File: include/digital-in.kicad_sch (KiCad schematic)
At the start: 6 parts, among them U9 EL817

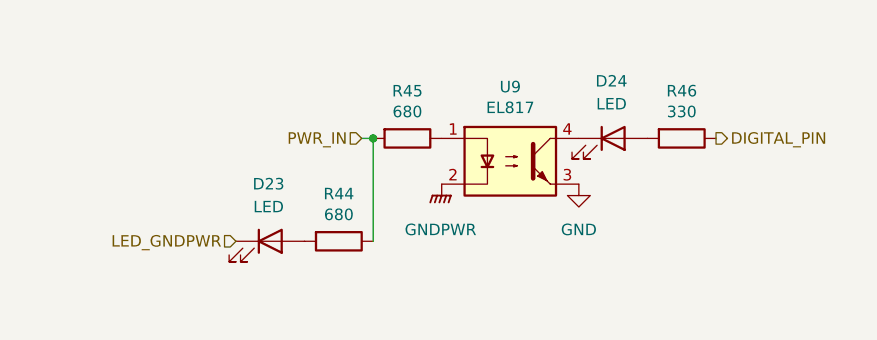
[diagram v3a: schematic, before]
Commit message: refactoring slave-8in-8out
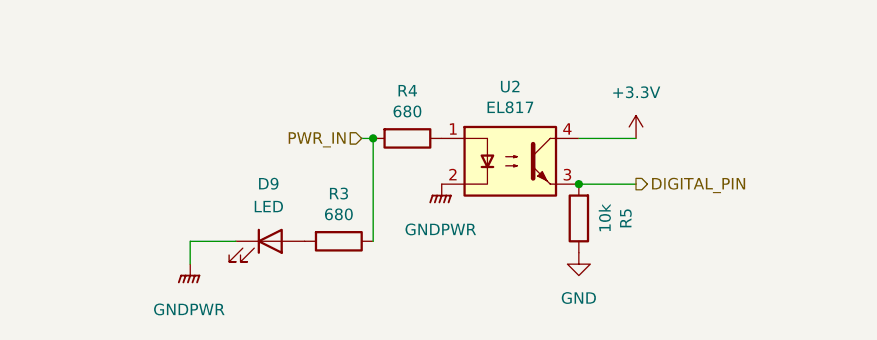
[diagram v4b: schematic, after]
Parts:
- removed D24: LED, Resistor_SMD:R_0805_2012Metric, symbol Device:LED
- R5: renamed from R46; value 330 -> 10k; LCSC C25117 -> C25744
- renumbered D23 to D9, R44 to R3, R45 to R4, U9 to U2
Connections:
- net LED_GNDPWR is gone; now on net GNDPWR: D9.1 (K)
- net DIGITAL_PIN: now also R5.2, U2.3; no longer R5.1
- net GND: now also R5.1; no longer U2.3
- net +3V3: now reaches U2.4
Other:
- moved on the sheet: R5
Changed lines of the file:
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@@
   (paper "A4")
   (junction (at 74.93 36.83) (diameter 0.9144) (color 0 0 0 0))
+  (junction (at 97.79 41.91) (diameter 0) (color 0 0 0 0))
+  (wire (pts (xy 54.61 48.26) (xy 54.61 50.8))
+    (stroke (width 0) (type default) (color 0 0 0 0))
+  )
+  (wire (pts (xy 59.69 48.26) (xy 54.61 48.26))
+    (stroke (width 0) (type default) (color 0 0 0 0))
+  )
   (wire (pts (xy 73.66 36.83) (xy 74.93 36.83))
     (stroke (width 0) (type solid) (color 0 0 0 0))
@@
     (stroke (width 0) (type solid) (color 0 0 0 0))
   )
-  (hierarchical_label "LED_GNDPWR" (shape input) (at 59.69 48.26 180)
-    (effects (font (size 1.27 1.27)) (justify right))
+  (wire (pts (xy 97.79 36.83) (xy 104.14 36.83))
+    (stroke (width 0) (type default) (color 0 0 0 0))
+  )
+  (wire (pts (xy 97.79 41.91) (xy 104.14 41.91))
+    (stroke (width 0) (type default) (color 0 0 0 0))
   )
   (hierarchical_label "PWR_IN" (shape input) (at 73.66 36.83 180)
     (effects (font (size 1.27 1.27)) (justify right))
   )
-  (hierarchical_label "DIGITAL_PIN" (shape output) (at 113.03 36.83 0)
+  (hierarchical_label "DIGITAL_PIN" (shape output) (at 104.14 41.91 0)
     (effects (font (size 1.27 1.27)) (justify left))
+  )
+  (symbol (lib_id "power:+3.3V") (at 104.14 36.83 0)
+    (in_bom yes) (on_board yes) (fields_autoplaced)
+    (property "Reference" "#PWR0126" (id 0) (at 104.14 40.64 0)
+      (effects (font (size 1.27 1.27)) hide)
+    )
+    (property "Value" "+3.3V" (id 1) (at 104.14 31.75 0))
+    (property "Footprint" "" (id 2) (at 104.14 36.83 0)
+      (effects (font (size 1.27 1.27)) hide)
+    )
+    (property "Datasheet" "" (id 3) (at 104.14 36.83 0)
+      (effects (font (size 1.27 1.27)) hide)
+    )
+    (pin "1")
+  )
+  (symbol (lib_id "power:GNDPWR") (at 54.61 50.8 0)
+    (in_bom yes) (on_board yes) (fields_autoplaced)
+    (property "Reference" "#PWR0134" (id 0) (at 54.61 55.88 0)
+      (effects (font (size 1.27 1.27)) hide)
+    )
+    (property "Value" "GNDPWR" (id 1) (at 54.483 55.88 0))
+    (property "Footprint" "" (id 2) (at 54.61 52.07 0)
+      (effects (font (size 1.27 1.27)) hide)
+    )
+    (property "Datasheet" "" (id 3) (at 54.61 52.07 0)
+      (effects (font (size 1.27 1.27)) hide)
+    )
+    (pin "1")
   )
   (symbol (lib_id "power:GNDPWR") (at 82.55 41.91 0)
@@
     (pin "1")
   )
-  (symbol (lib_id "power:GND") (at 97.79 41.91 0)
+  (symbol (lib_id "power:GND") (at 97.79 49.53 0)
     (in_bom yes) (on_board yes) (fields_autoplaced)
-    (property "Reference" "#PWR0116" (id 0) (at 97.79 48.26 0)
+    (property "Reference" "#PWR0116" (id 0) (at 97.79 55.88 0)
       (effects (font (size 1.27 1.27)) hide)
     )
-    (property "Value" "GND" (id 1) (at 97.79 46.99 0))
-    (property "Footprint" "" (id 2) (at 97.79 41.91 0)
+    (property "Value" "GND" (id 1) (at 97.79 54.61 0))
+    (property "Footprint" "" (id 2) (at 97.79 49.53 0)
       (effects (font (size 1.27 1.27)) hide)
     )
-    (property "Datasheet" "" (id 3) (at 97.79 41.91 0)
+    (property "Datasheet" "" (id 3) (at 97.79 49.53 0)
       (effects (font (size 1.27 1.27)) hide)
     )
@@
   (symbol (lib_id "Device:R") (at 71.12 48.26 270)
     (in_bom yes) (on_board yes)
-    (property "Reference" "R44" (id 0) (at 71.12 43.0022 90))
+    (property "Reference" "R3" (id 0) (at 71.12 43.0022 90))
     (property "Value" "680" (id 1) (at 71.12 45.3136 90))
     (property "Footprint" "Resistor_SMD:R_0402_1005Metric" (id 2) (at 71.12 46.482 90)
@@
   (symbol (lib_id "Device:R") (at 78.74 36.83 270)
     (in_bom yes) (on_board yes)
-    (property "Reference" "R45" (id 0) (at 78.74 31.5722 90))
+    (property "Reference" "R4" (id 0) (at 78.74 31.5722 90))
     (property "Value" "680" (id 1) (at 78.74 33.8836 90))
     (property "Footprint" "Resistor_SMD:R_0402_1005Metric" (id 2) (at 78.74 35.052 90)
@@
     (pin "2")
   )
-  (symbol (lib_id "Device:R") (at 109.22 36.83 270)
+  (symbol (lib_id "Device:R") (at 97.79 45.72 180)
     (in_bom yes) (on_board yes)
-    (property "Reference" "R46" (id 0) (at 109.22 31.5722 90))
-    (property "Value" "330" (id 1) (at 109.22 33.8836 90))
-    (property "Footprint" "Resistor_SMD:R_0402_1005Metric" (id 2) (at 109.22 35.052 90)
+    (property "Reference" "R5" (id 0) (at 103.0478 45.72 90))
+    (property "Value" "10k" (id 1) (at 100.7364 45.72 90))
+    (property "Footprint" "Resistor_SMD:R_0402_1005Metric" (id 2) (at 99.568 45.72 90)
       (effects (font (size 1.27 1.27)) hide)
     )
-    (property "Datasheet" "https://datasheet.lcsc.com/lcsc/1810170414_UNI-ROYAL-Uniroyal-Elec-0402WGF4700TCE_C25117.pdf" (id 3) (at 109.22 36.83 0)
+    (property "Datasheet" "https://datasheet.lcsc.com/lcsc/1809301717_UNI-ROYAL-Uniroyal-Elec-0402WGF1002TCE_C25744.pdf" (id 3) (at 97.79 45.72 0)
       (effects (font (size 1.27 1.27)) hide)
     )
-    (property "LCSC" "C25117" (id 4) (at 109.22 36.83 90)
+    (property "LCSC" "C25744" (id 4) (at 97.79 45.72 90)
       (effects (font (size 1.27 1.27)) hide)
     )
@@
   (symbol (lib_id "Device:LED") (at 63.5 48.26 0)
     (in_bom yes) (on_board yes) (fields_autoplaced)
-    (property "Reference" "D23" (id 0) (at 63.3095 41.91 0))
+    (property "Reference" "D9" (id 0) (at 63.3095 41.91 0))
     (property "Value" "LED" (id 1) (at 63.3095 44.45 0))
     (property "Footprint" "Resistor_SMD:R_0805_2012Metric" (id 2) (at 63.5 48.26 0)
@@
     (pin "2")
   )
-  (symbol (lib_id "Device:LED") (at 101.6 36.83 0)
-    (in_bom yes) (on_board yes) (fields_autoplaced)
-    (property "Reference" "D24" (id 0) (at 101.4095 30.48 0))
-    (property "Value" "LED" (id 1) (at 101.4095 33.02 0))
-    (property "Footprint" "Resistor_SMD:R_0805_2012Metric" (id 2) (at 101.6 36.83 0)
-      (effects (font (size 1.27 1.27)) hide)
-    )
-    (property "Datasheet" "https://datasheet.lcsc.com/lcsc/2008201032_Foshan-NationStar-Optoelectronics-NCD0805R1_C84256.pdf" (id 3) (at 101.6 36.83 0)
-      (effects (font (size 1.27 1.27)) hide)
-    )
-    (property "LCSC" "C84256" (id 4) (at 101.6 36.83 0)
-      (effects (font (size 1.27 1.27)) hide)
-    )
-    (pin "1")
-    (pin "2")
-  )
   (symbol (lib_id "jlcpcb:EL817") (at 90.17 39.37 0)
     (in_bom yes) (on_board yes)
-    (property "Reference" "U9" (id 0) (at 90.17 31.115 0))
+    (property "Reference" "U2" (id 0) (at 90.17 31.115 0))
     (property "Value" "EL817" (id 1) (at 90.17 33.4264 0))
     (property "Footprint" "jlcpcb:EL817" (id 2) (at 111.76 44.45 0)

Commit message: update slave-8in-8out
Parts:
- renumbered D9 to D23, R3 to R44, R4 to R45, R5 to R46, U2 to U9
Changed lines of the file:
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@@
   (symbol (lib_id "Device:R") (at 71.12 48.26 270)
     (in_bom yes) (on_board yes)
-    (property "Reference" "R3" (id 0) (at 71.12 43.0022 90))
+    (property "Reference" "R44" (id 0) (at 71.12 43.0022 90))
     (property "Value" "680" (id 1) (at 71.12 45.3136 90))
     (property "Footprint" "Resistor_SMD:R_0402_1005Metric" (id 2) (at 71.12 46.482 90)
@@
   (symbol (lib_id "Device:R") (at 78.74 36.83 270)
     (in_bom yes) (on_board yes)
-    (property "Reference" "R4" (id 0) (at 78.74 31.5722 90))
+    (property "Reference" "R45" (id 0) (at 78.74 31.5722 90))
     (property "Value" "680" (id 1) (at 78.74 33.8836 90))
     (property "Footprint" "Resistor_SMD:R_0402_1005Metric" (id 2) (at 78.74 35.052 90)
@@
   (symbol (lib_id "Device:R") (at 97.79 45.72 180)
     (in_bom yes) (on_board yes)
-    (property "Reference" "R5" (id 0) (at 103.0478 45.72 90))
+    (property "Reference" "R46" (id 0) (at 103.0478 45.72 90))
     (property "Value" "10k" (id 1) (at 100.7364 45.72 90))
     (property "Footprint" "Resistor_SMD:R_0402_1005Metric" (id 2) (at 99.568 45.72 90)
@@
   (symbol (lib_id "Device:LED") (at 63.5 48.26 0)
     (in_bom yes) (on_board yes) (fields_autoplaced)
-    (property "Reference" "D9" (id 0) (at 63.3095 41.91 0))
+    (property "Reference" "D23" (id 0) (at 63.3095 41.91 0))
     (property "Value" "LED" (id 1) (at 63.3095 44.45 0))
     (property "Footprint" "Resistor_SMD:R_0805_2012Metric" (id 2) (at 63.5 48.26 0)
@@
   (symbol (lib_id "jlcpcb:EL817") (at 90.17 39.37 0)
     (in_bom yes) (on_board yes)
-    (property "Reference" "U2" (id 0) (at 90.17 31.115 0))
+    (property "Reference" "U9" (id 0) (at 90.17 31.115 0))
     (property "Value" "EL817" (id 1) (at 90.17 33.4264 0))
     (property "Footprint" "jlcpcb:EL817" (id 2) (at 111.76 44.45 0)

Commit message: update slave-8in-8out
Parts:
- renumbered D23 to D9, R44 to R3, R45 to R4, R46 to R5, U9 to U2
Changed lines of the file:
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@@
   (symbol (lib_id "power:+3.3V") (at 104.14 36.83 0)
     (in_bom yes) (on_board yes) (fields_autoplaced)
-    (property "Reference" "#PWR0126" (id 0) (at 104.14 40.64 0)
+    (property "Reference" "#PWR0119" (id 0) (at 104.14 40.64 0)
       (effects (font (size 1.27 1.27)) hide)
     )
@@
   (symbol (lib_id "power:GNDPWR") (at 54.61 50.8 0)
     (in_bom yes) (on_board yes) (fields_autoplaced)
-    (property "Reference" "#PWR0134" (id 0) (at 54.61 55.88 0)
+    (property "Reference" "#PWR0127" (id 0) (at 54.61 55.88 0)
       (effects (font (size 1.27 1.27)) hide)
     )
@@
   (symbol (lib_id "power:GNDPWR") (at 82.55 41.91 0)
     (in_bom yes) (on_board yes) (fields_autoplaced)
-    (property "Reference" "#PWR0115" (id 0) (at 82.55 46.99 0)
+    (property "Reference" "#PWR0101" (id 0) (at 82.55 46.99 0)
       (effects (font (size 1.27 1.27)) hide)
     )
@@
   (symbol (lib_id "power:GND") (at 97.79 49.53 0)
     (in_bom yes) (on_board yes) (fields_autoplaced)
-    (property "Reference" "#PWR0116" (id 0) (at 97.79 55.88 0)
+    (property "Reference" "#PWR0102" (id 0) (at 97.79 55.88 0)
       (effects (font (size 1.27 1.27)) hide)
     )
@@
   (symbol (lib_id "Device:R") (at 71.12 48.26 270)
     (in_bom yes) (on_board yes)
-    (property "Reference" "R44" (id 0) (at 71.12 43.0022 90))
+    (property "Reference" "R3" (id 0) (at 71.12 43.0022 90))
     (property "Value" "680" (id 1) (at 71.12 45.3136 90))
     (property "Footprint" "Resistor_SMD:R_0402_1005Metric" (id 2) (at 71.12 46.482 90)
@@
   (symbol (lib_id "Device:R") (at 78.74 36.83 270)
     (in_bom yes) (on_board yes)
-    (property "Reference" "R45" (id 0) (at 78.74 31.5722 90))
+    (property "Reference" "R4" (id 0) (at 78.74 31.5722 90))
     (property "Value" "680" (id 1) (at 78.74 33.8836 90))
     (property "Footprint" "Resistor_SMD:R_0402_1005Metric" (id 2) (at 78.74 35.052 90)
@@
   (symbol (lib_id "Device:R") (at 97.79 45.72 180)
     (in_bom yes) (on_board yes)
-    (property "Reference" "R46" (id 0) (at 103.0478 45.72 90))
+    (property "Reference" "R5" (id 0) (at 103.0478 45.72 90))
     (property "Value" "10k" (id 1) (at 100.7364 45.72 90))
     (property "Footprint" "Resistor_SMD:R_0402_1005Metric" (id 2) (at 99.568 45.72 90)
@@
   (symbol (lib_id "Device:LED") (at 63.5 48.26 0)
     (in_bom yes) (on_board yes) (fields_autoplaced)
-    (property "Reference" "D23" (id 0) (at 63.3095 41.91 0))
+    (property "Reference" "D9" (id 0) (at 63.3095 41.91 0))
     (property "Value" "LED" (id 1) (at 63.3095 44.45 0))
     (property "Footprint" "Resistor_SMD:R_0805_2012Metric" (id 2) (at 63.5 48.26 0)
@@
   (symbol (lib_id "jlcpcb:EL817") (at 90.17 39.37 0)
     (in_bom yes) (on_board yes)
-    (property "Reference" "U9" (id 0) (at 90.17 31.115 0))
+    (property "Reference" "U2" (id 0) (at 90.17 31.115 0))
     (property "Value" "EL817" (id 1) (at 90.17 33.4264 0))
     (property "Footprint" "jlcpcb:EL817" (id 2) (at 111.76 44.45 0)

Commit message: update slave-8in-8out routing
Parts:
- D9: footprint Resistor_SMD:R_0805_2012Metric -> LED_SMD:LED_0805_2012Metric
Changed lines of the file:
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@@
     (property "Reference" "D9" (id 0) (at 63.3095 41.91 0))
     (property "Value" "LED" (id 1) (at 63.3095 44.45 0))
-    (property "Footprint" "Resistor_SMD:R_0805_2012Metric" (id 2) (at 63.5 48.26 0)
+    (property "Footprint" "LED_SMD:LED_0805_2012Metric" (id 2) (at 63.5 48.26 0)
       (effects (font (size 1.27 1.27)) hide)
     )

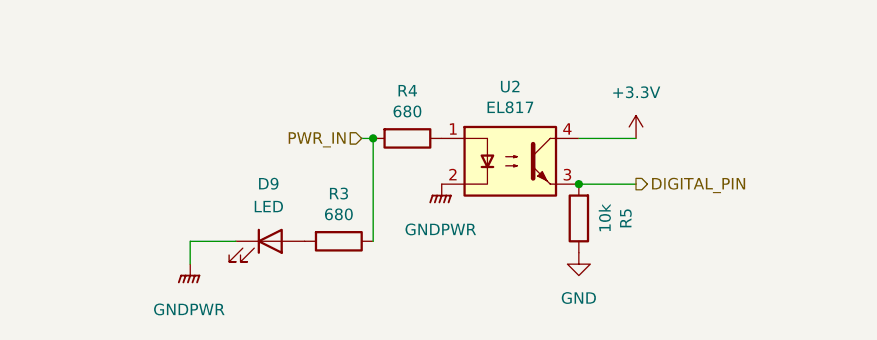
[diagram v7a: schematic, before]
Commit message: update slave-8in-8out routing
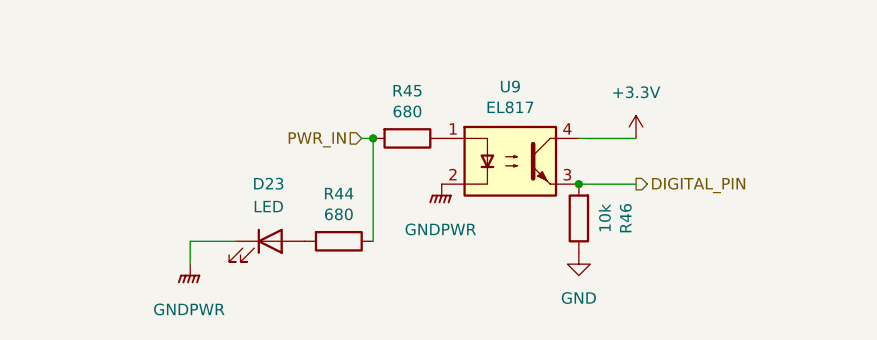
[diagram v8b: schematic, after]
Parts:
- renumbered D9 to D23, R3 to R44, R4 to R45, R5 to R46, U2 to U9
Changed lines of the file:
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@@
   (symbol (lib_id "power:+3.3V") (at 104.14 36.83 0)
     (in_bom yes) (on_board yes) (fields_autoplaced)
-    (property "Reference" "#PWR0119" (id 0) (at 104.14 40.64 0)
+    (property "Reference" "#PWR0126" (id 0) (at 104.14 40.64 0)
       (effects (font (size 1.27 1.27)) hide)
     )
@@
   (symbol (lib_id "power:GNDPWR") (at 54.61 50.8 0)
     (in_bom yes) (on_board yes) (fields_autoplaced)
-    (property "Reference" "#PWR0127" (id 0) (at 54.61 55.88 0)
+    (property "Reference" "#PWR0134" (id 0) (at 54.61 55.88 0)
       (effects (font (size 1.27 1.27)) hide)
     )
@@
   (symbol (lib_id "power:GNDPWR") (at 82.55 41.91 0)
     (in_bom yes) (on_board yes) (fields_autoplaced)
-    (property "Reference" "#PWR0101" (id 0) (at 82.55 46.99 0)
+    (property "Reference" "#PWR0115" (id 0) (at 82.55 46.99 0)
       (effects (font (size 1.27 1.27)) hide)
     )
@@
   (symbol (lib_id "power:GND") (at 97.79 49.53 0)
     (in_bom yes) (on_board yes) (fields_autoplaced)
-    (property "Reference" "#PWR0102" (id 0) (at 97.79 55.88 0)
+    (property "Reference" "#PWR0116" (id 0) (at 97.79 55.88 0)
       (effects (font (size 1.27 1.27)) hide)
     )
@@
   (symbol (lib_id "Device:R") (at 71.12 48.26 270)
     (in_bom yes) (on_board yes)
-    (property "Reference" "R3" (id 0) (at 71.12 43.0022 90))
+    (property "Reference" "R44" (id 0) (at 71.12 43.0022 90))
     (property "Value" "680" (id 1) (at 71.12 45.3136 90))
     (property "Footprint" "Resistor_SMD:R_0402_1005Metric" (id 2) (at 71.12 46.482 90)
@@
   (symbol (lib_id "Device:R") (at 78.74 36.83 270)
     (in_bom yes) (on_board yes)
-    (property "Reference" "R4" (id 0) (at 78.74 31.5722 90))
+    (property "Reference" "R45" (id 0) (at 78.74 31.5722 90))
     (property "Value" "680" (id 1) (at 78.74 33.8836 90))
     (property "Footprint" "Resistor_SMD:R_0402_1005Metric" (id 2) (at 78.74 35.052 90)
@@
   (symbol (lib_id "Device:R") (at 97.79 45.72 180)
     (in_bom yes) (on_board yes)
-    (property "Reference" "R5" (id 0) (at 103.0478 45.72 90))
+    (property "Reference" "R46" (id 0) (at 103.0478 45.72 90))
     (property "Value" "10k" (id 1) (at 100.7364 45.72 90))
     (property "Footprint" "Resistor_SMD:R_0402_1005Metric" (id 2) (at 99.568 45.72 90)
@@
   (symbol (lib_id "Device:LED") (at 63.5 48.26 0)
     (in_bom yes) (on_board yes) (fields_autoplaced)
-    (property "Reference" "D9" (id 0) (at 63.3095 41.91 0))
+    (property "Reference" "D23" (id 0) (at 63.3095 41.91 0))
     (property "Value" "LED" (id 1) (at 63.3095 44.45 0))
     (property "Footprint" "LED_SMD:LED_0805_2012Metric" (id 2) (at 63.5 48.26 0)
@@
   (symbol (lib_id "jlcpcb:EL817") (at 90.17 39.37 0)
     (in_bom yes) (on_board yes)
-    (property "Reference" "U2" (id 0) (at 90.17 31.115 0))
+    (property "Reference" "U9" (id 0) (at 90.17 31.115 0))
     (property "Value" "EL817" (id 1) (at 90.17 33.4264 0))
     (property "Footprint" "jlcpcb:EL817" (id 2) (at 111.76 44.45 0)
